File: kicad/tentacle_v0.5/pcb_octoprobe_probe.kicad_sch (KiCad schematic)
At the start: 23 parts, among them J1501 Conn_02x20, J1502 Conn_01x12, U1501 RP2040, U1502 W25Q32JVS, U1503 TXB0108PW

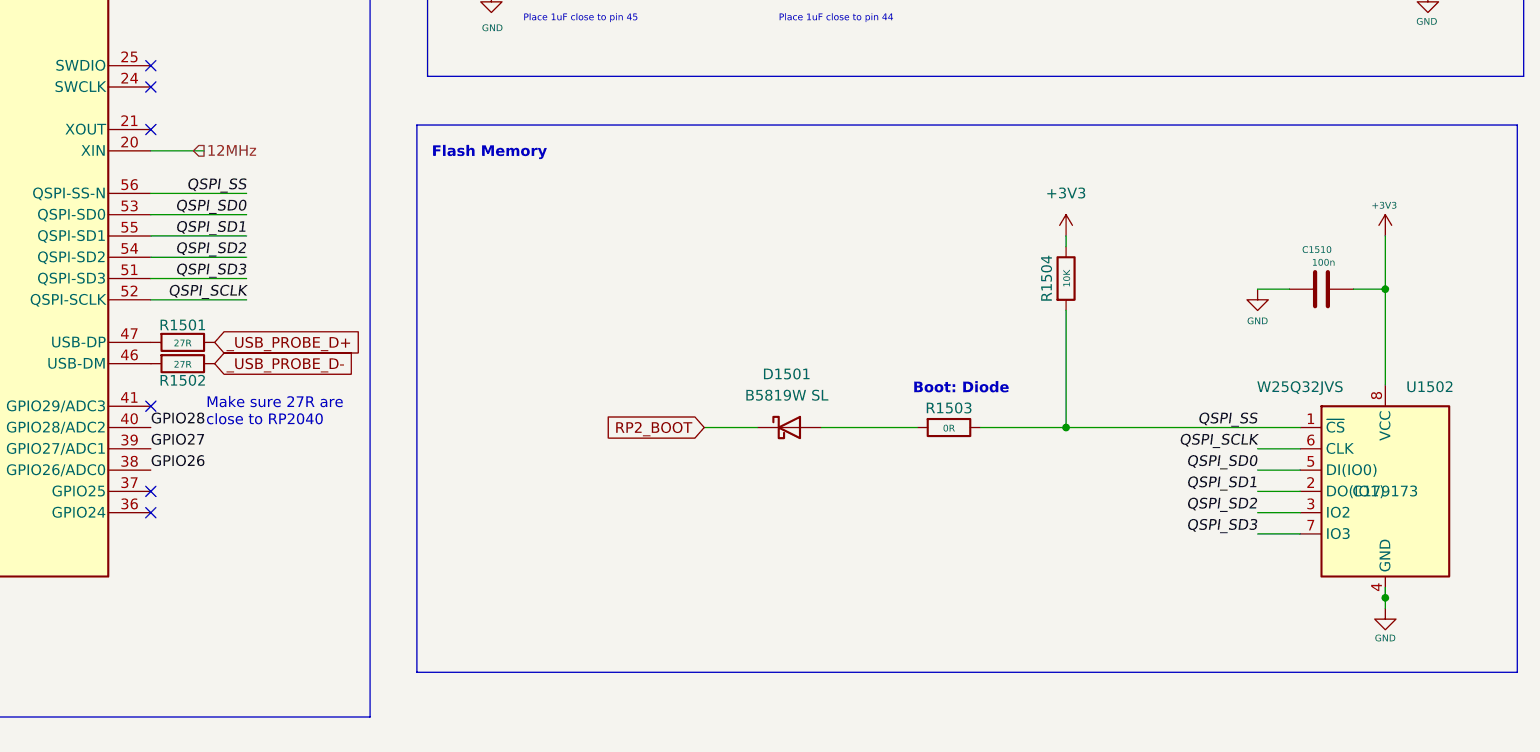
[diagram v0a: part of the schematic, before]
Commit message: Schematics: Fix ERC warnings
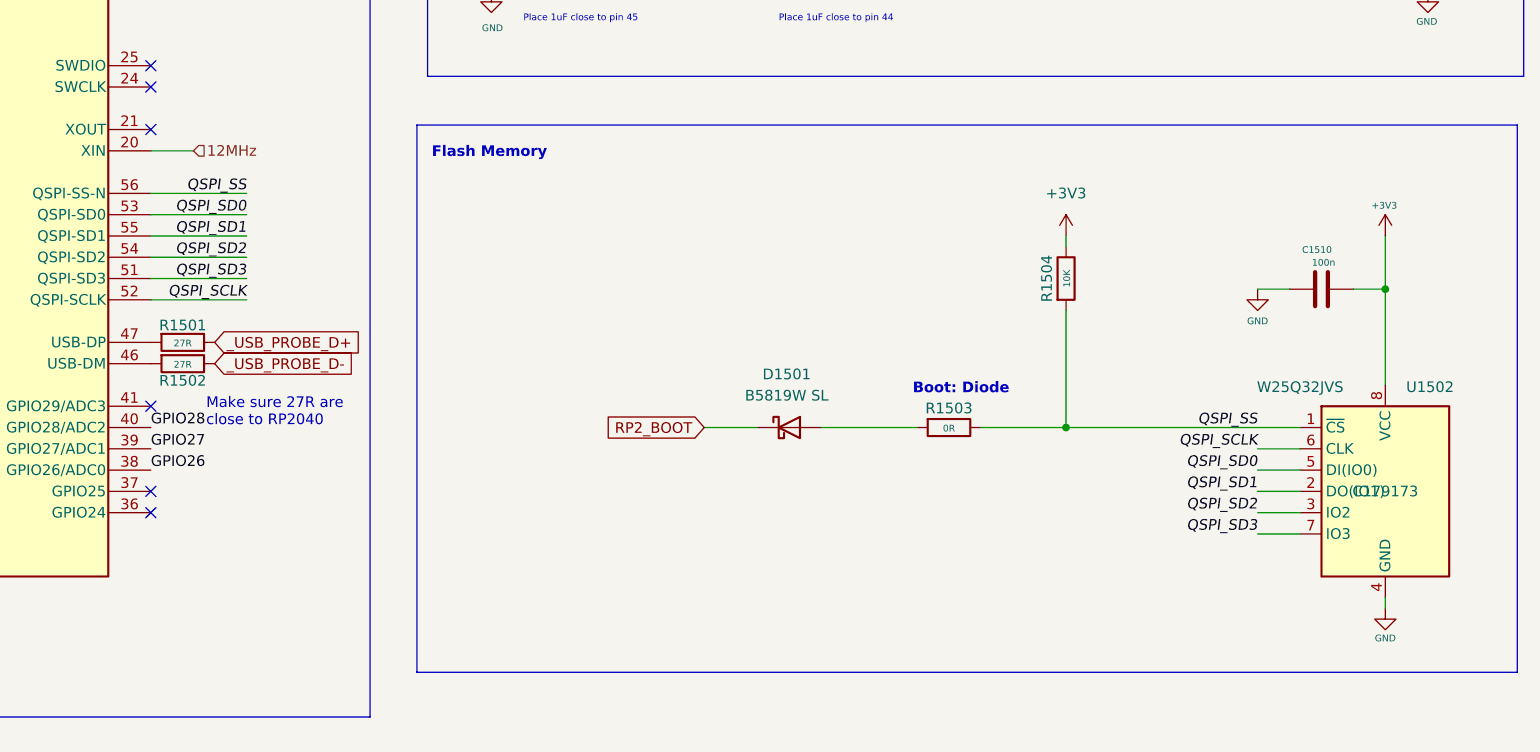
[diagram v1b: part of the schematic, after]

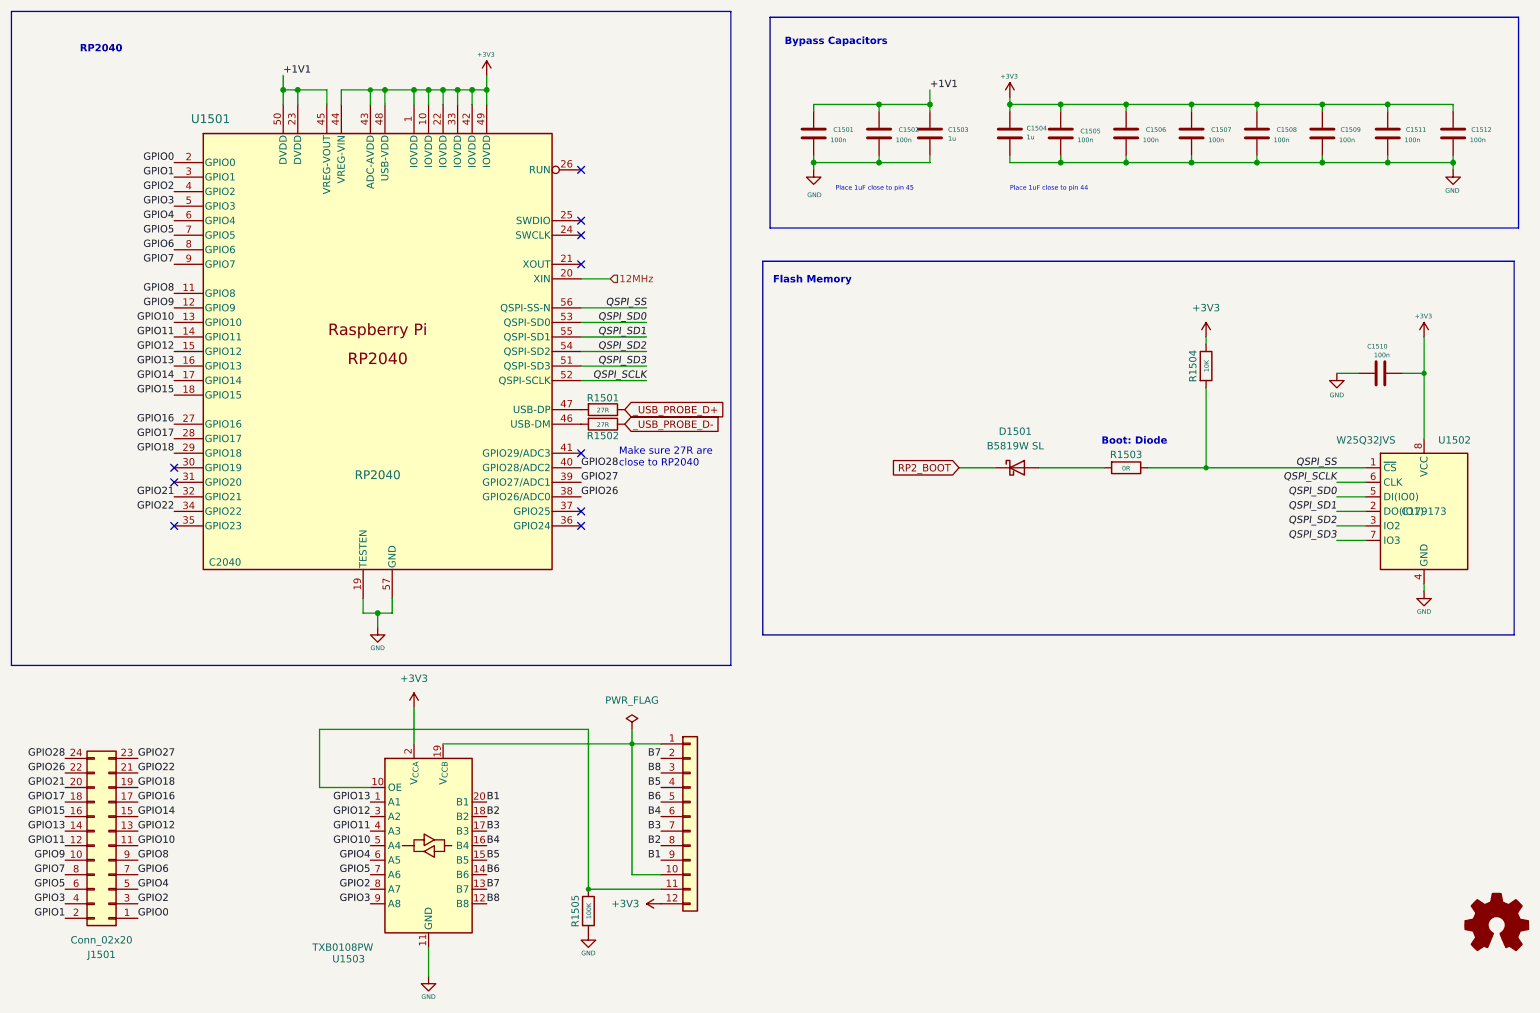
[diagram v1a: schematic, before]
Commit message: Breadboard: Remove pads from schematic
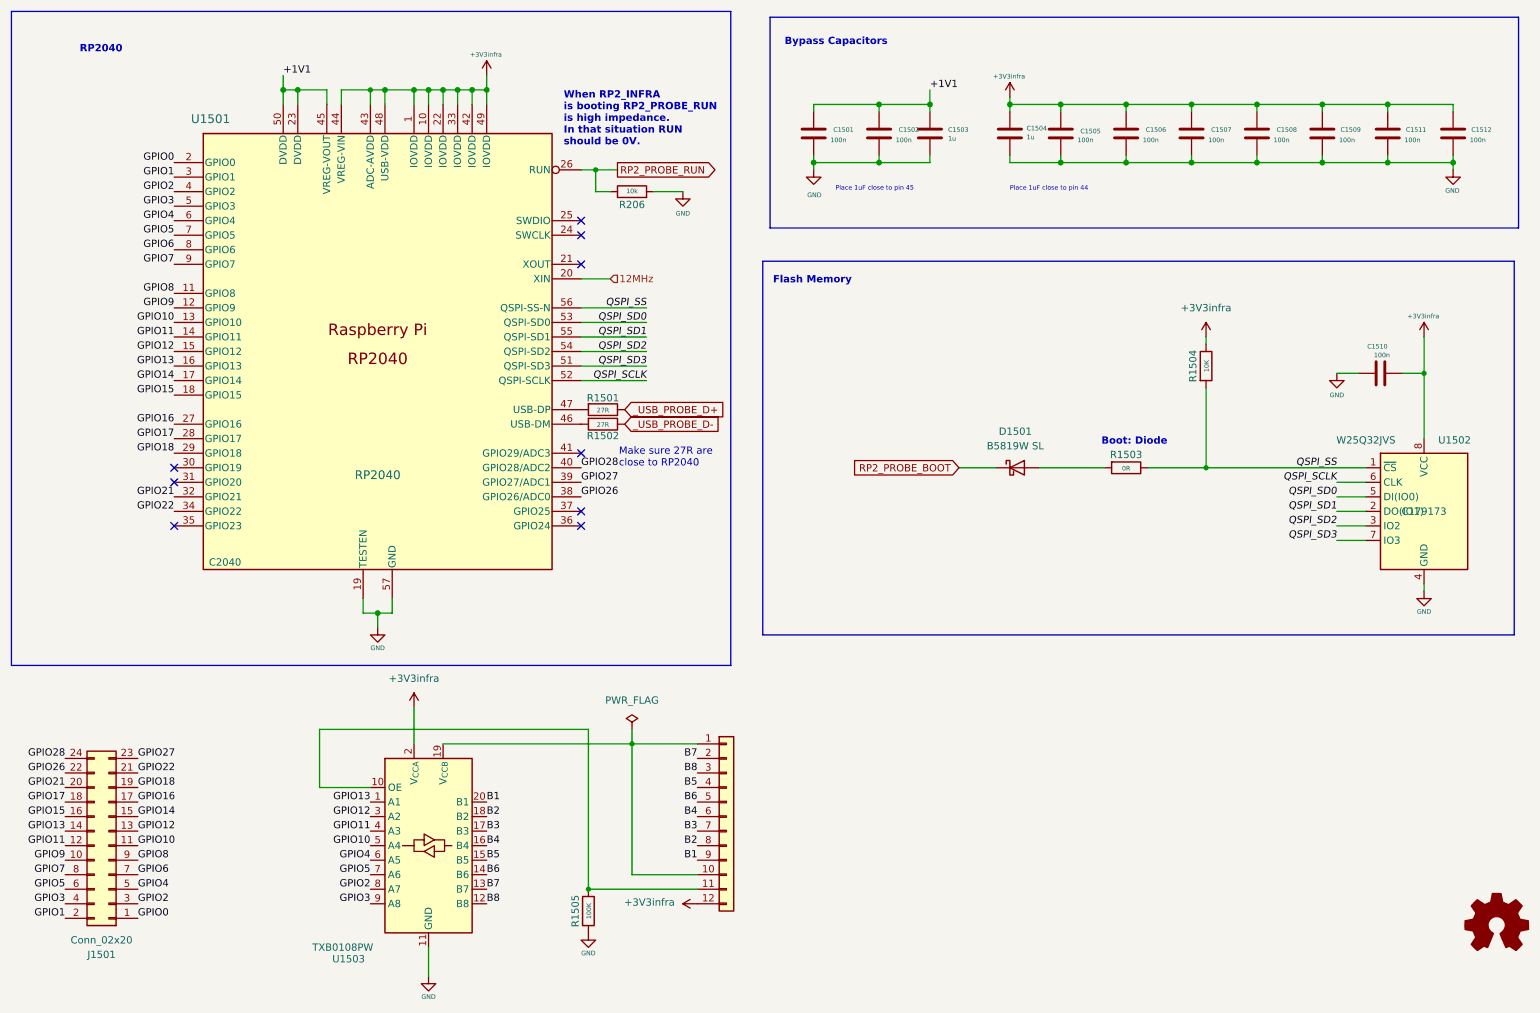
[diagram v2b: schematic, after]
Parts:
- added R206: 10k, Resistor_SMD:R_0402_1005Metric, symbol Device:R
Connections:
- net GND: now also R206.2
- net RP2_PROBE_RUN: now reaches U1501.26 (RUN)
- net RP2_PROBE_RUN: now also R206.1
- net +3V3 renamed +3V3infra
- net RP2_BOOT renamed RP2_PROBE_BOOT
- no-connect marks 10 -> 9
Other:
- note added: "When RP2_INFRA is booting RP2_PROBE_RUN is high impedance. In that situation RUN should be 0V."

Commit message: tentacle v0.5 kicad - unknown small changes to schematics
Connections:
- net VDUT: now reaches J1502.1 (Pin_1), J1502.10 (Pin_10), U1503.19 (V_{CCB})
- net OE: now reaches J1502.11 (Pin_11), R1505.1, U1503.10 (OE)
- net B1 renamed 13
- net B2 renamed 12
- net B3 renamed 11
- net B4 renamed 10
- net B5 renamed 4
- net B6 renamed 5
- net B7 renamed 2
- net B8 renamed 3
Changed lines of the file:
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@@
+	(wire
+		(pts
+			(xy 147.32 161.29) (xy 135.89 161.29)
+		)
+		(stroke
+			(width 0)
+			(type default)
+		)
+	)
 	(wire
 		(pts
@@
 	(wire
 		(pts
+			(xy 147.32 163.83) (xy 135.89 163.83)
+		)
+		(stroke
+			(width 0)
+			(type default)
+		)
+	)
+	(wire
+		(pts
 			(xy 80.01 120.65) (xy 82.55 120.65)
 		)
@@
 	(wire
 		(pts
-			(xy 124.46 143.51) (xy 135.89 143.51)
+			(xy 124.46 143.51) (xy 147.32 143.51)
 		)
 		(stroke
@@
 	(wire
 		(pts
+			(xy 147.32 148.59) (xy 135.89 148.59)
+		)
+		(stroke
+			(width 0)
+			(type default)
+		)
+	)
+	(wire
+		(pts
 			(xy 78.74 31.75) (xy 78.74 29.21)
 		)
@@
 	(wire
 		(pts
+			(xy 147.32 151.13) (xy 135.89 151.13)
+		)
+		(stroke
+			(width 0)
+			(type default)
+		)
+	)
+	(wire
+		(pts
 			(xy 245.11 40.64) (xy 245.11 41.91)
 		)
@@
 	(wire
 		(pts
+			(xy 147.32 156.21) (xy 135.89 156.21)
+		)
+		(stroke
+			(width 0)
+			(type default)
+		)
+	)
+	(wire
+		(pts
 			(xy 66.04 31.75) (xy 66.04 29.21)
 		)
@@
 	(wire
 		(pts
-			(xy 124.46 166.37) (xy 135.89 166.37)
+			(xy 124.46 166.37) (xy 147.32 166.37)
 		)
 		(stroke
@@
 	(wire
 		(pts
+			(xy 147.32 153.67) (xy 135.89 153.67)
+		)
+		(stroke
+			(width 0)
+			(type default)
+		)
+	)
+	(wire
+		(pts
 			(xy 210.82 33.02) (xy 210.82 31.75)
 		)
@@
 	(wire
 		(pts
+			(xy 147.32 146.05) (xy 135.89 146.05)
+		)
+		(stroke
+			(width 0)
+			(type default)
+		)
+	)
+	(wire
+		(pts
 			(xy 88.9 31.75) (xy 88.9 29.21)
 		)
@@
 	(wire
 		(pts
-			(xy 116.84 168.91) (xy 135.89 168.91)
+			(xy 116.84 168.91) (xy 147.32 168.91)
 		)
 		(stroke
@@
 	(wire
 		(pts
+			(xy 147.32 158.75) (xy 135.89 158.75)
+		)
+		(stroke
+			(width 0)
+			(type default)
+		)
+	)
+	(wire
+		(pts
 			(xy 190.5 30.48) (xy 190.5 31.75)
 		)
@@
 			(width 0)
 			(type solid)
+		)
+	)
+	(wire
+		(pts
+			(xy 135.89 171.45) (xy 147.32 171.45)
+		)
+		(stroke
+			(width 0)
+			(type default)
 		)
 	)
@@
 		)
 	)
+	(label "VDUT"
+		(at 144.78 166.37 180)
+		(effects
+			(font
+				(size 1.27 1.27)
+			)
+			(justify right bottom)
+		)
+	)
 	(label "GPIO18"
 		(at 44.45 92.71 180)
@@
 		)
 	)
+	(label "13"
+		(at 144.78 163.83 180)
+		(effects
+			(font
+				(size 1.27 1.27)
+			)
+			(justify right bottom)
+		)
+	)
 	(label "GPIO2"
 		(at 44.45 46.99 180)
@@
 		)
 	)
+	(label "10"
+		(at 144.746 156.21 180)
+		(effects
+			(font
+				(size 1.27 1.27)
+			)
+			(justify right bottom)
+		)
+	)
 	(label "B3"
 		(at 99.06 158.75 0)
@@
 		)
 	)
+	(label "2"
+		(at 144.78 146.05 180)
+		(effects
+			(font
+				(size 1.27 1.27)
+			)
+			(justify right bottom)
+		)
+	)
 	(label "GPIO3"
 		(at 78.74 171.45 180)
@@
 		)
 	)
+	(label "VDUT"
+		(at 144.78 143.51 180)
+		(effects
+			(font
+				(size 1.27 1.27)
+			)
+			(justify right bottom)
+		)
+	)
 	(label "GPIO18"
 		(at 38.1 151.13 0)
@@
 		)
 	)
+	(label "5"
+		(at 144.746 153.67 180)
+		(effects
+			(font
+				(size 1.27 1.27)
+			)
+			(justify right bottom)
+		)
+	)
+	(label "4"
+		(at 144.746 151.13 180)
+		(effects
+			(font
+				(size 1.27 1.27)
+			)
+			(justify right bottom)
+		)
+	)
 	(label "GPIO1"
 		(at 25.4 173.99 180)
@@
 		)
 	)
+	(label "3"
+		(at 144.7799 148.59 180)
+		(effects
+			(font
+				(size 1.27 1.27)
+			)
+			(justify right bottom)
+		)
+	)
 	(label "GPIO5"
 		(at 25.4 168.91 180)
@@
 		)
 	)
+	(label "12"
+		(at 144.78 161.29 180)
+		(effects
+			(font
+				(size 1.27 1.27)
+			)
+			(justify right bottom)
+		)
+	)
 	(label "GPIO3"
 		(at 44.45 49.53 180)
@@
 		)
 	)
+	(label "11"
+		(at 144.746 158.75 180)
+		(effects
+			(font
+				(size 1.27 1.27)
+			)
+			(justify right bottom)
+		)
+	)
 	(label "B5"
 		(at 135.89 151.13 180)
@@
 		)
 	)
+	(label "OE"
+		(at 144.78 168.91 180)
+		(effects
+			(font
+				(size 1.27 1.27)
+			)
+			(justify right bottom)
+		)
+	)
 	(label "GPIO15"
 		(at 25.4 156.21 180)
@@
 	)
 	(global_label "RP2_PROBE_RUN"
-		(shape output)
+		(shape input)
 		(at 121.92 43.18 0)
 		(fields_autoplaced yes)
@@
 	(symbol
 		(lib_id "Connector_Generic:Conn_01x12")
-		(at 140.97 156.21 0)
+		(at 152.4 156.21 0)
 		(unit 1)
 		(exclude_from_sim no)
@@
 		(fields_autoplaced yes)
 		(property "Reference" "J1502"
-			(at 143.51 156.2099 0)
+			(at 154.94 156.2099 0)
 			(effects
 				(font
@@
 		)
 		(property "Value" "Conn_01x12"
-			(at 143.51 158.7499 0)
+			(at 154.94 158.7499 0)
 			(effects
 				(font
@@
 		)
 		(property "Footprint" "00_project_library:PinSocket_1x12_P2.54mm_Vertical_squarepad"
-			(at 140.97 156.21 0)
+			(at 152.4 156.21 0)
 			(effects
 				(font
@@
 		)
 		(property "Datasheet" "~"
-			(at 140.97 156.21 0)
+			(at 152.4 156.21 0)
 			(effects
 				(font
@@
 		)
 		(property "Description" "Generic connector, single row, 01x12, script generated (kicad-library-utils/schlib/autogen/connector/)"
-			(at 140.97 156.21 0)
-			(effects
-				(font
+			(at 152.4 156.21 0)
+			(effects
+				(font
